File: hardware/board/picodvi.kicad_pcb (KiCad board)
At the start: 4 copper layers, 50 x 30 mm, 55 parts, among them J1 USB_OTG, J2 Conn_01x05, J3 02x06, J4 02x06, J5 NOT_HDMI_A, J6 Conn_01x02, SW1 SW_Push, SW2 SW_Push, SW3 SW_Push, U1 RP2040, U2 NCP115ASN330, U3 W25Q16JV, Y1 12 M

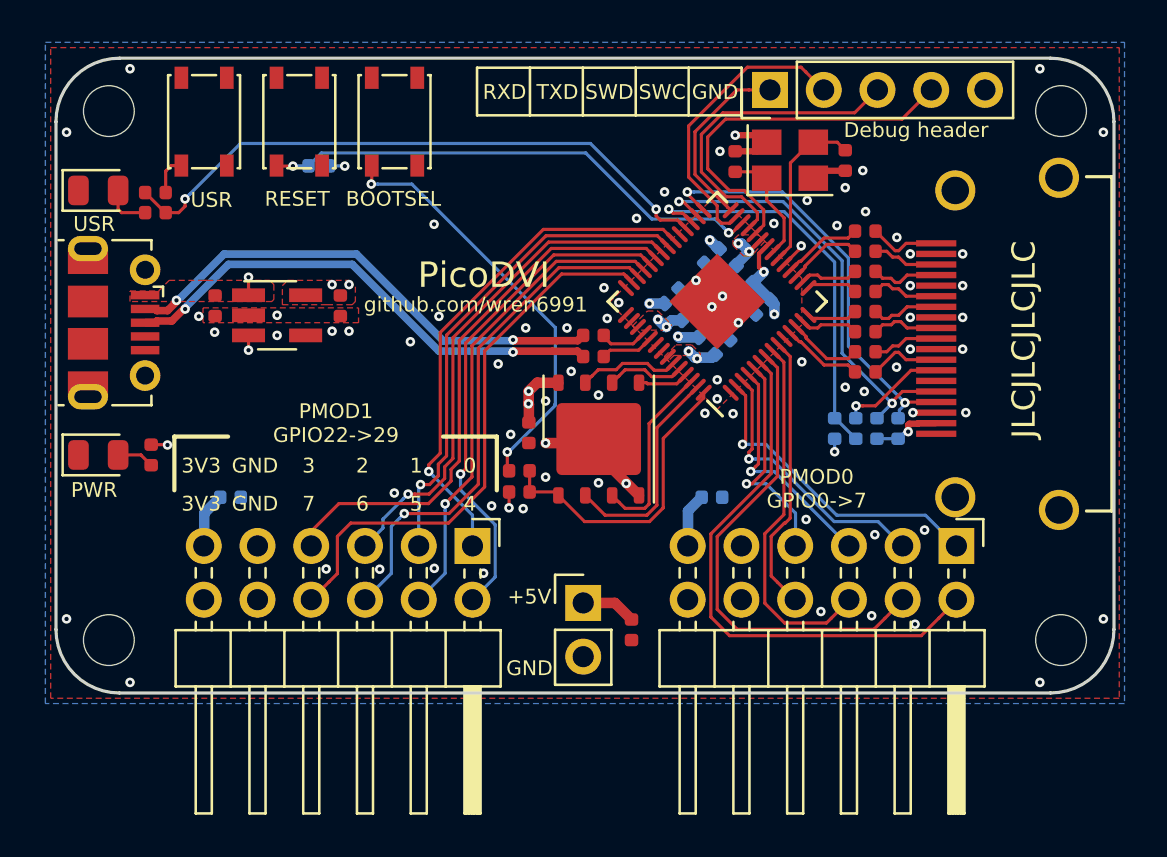
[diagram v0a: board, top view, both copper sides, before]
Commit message: Small updates to PCB
- USB-C
- Silkscreen lables
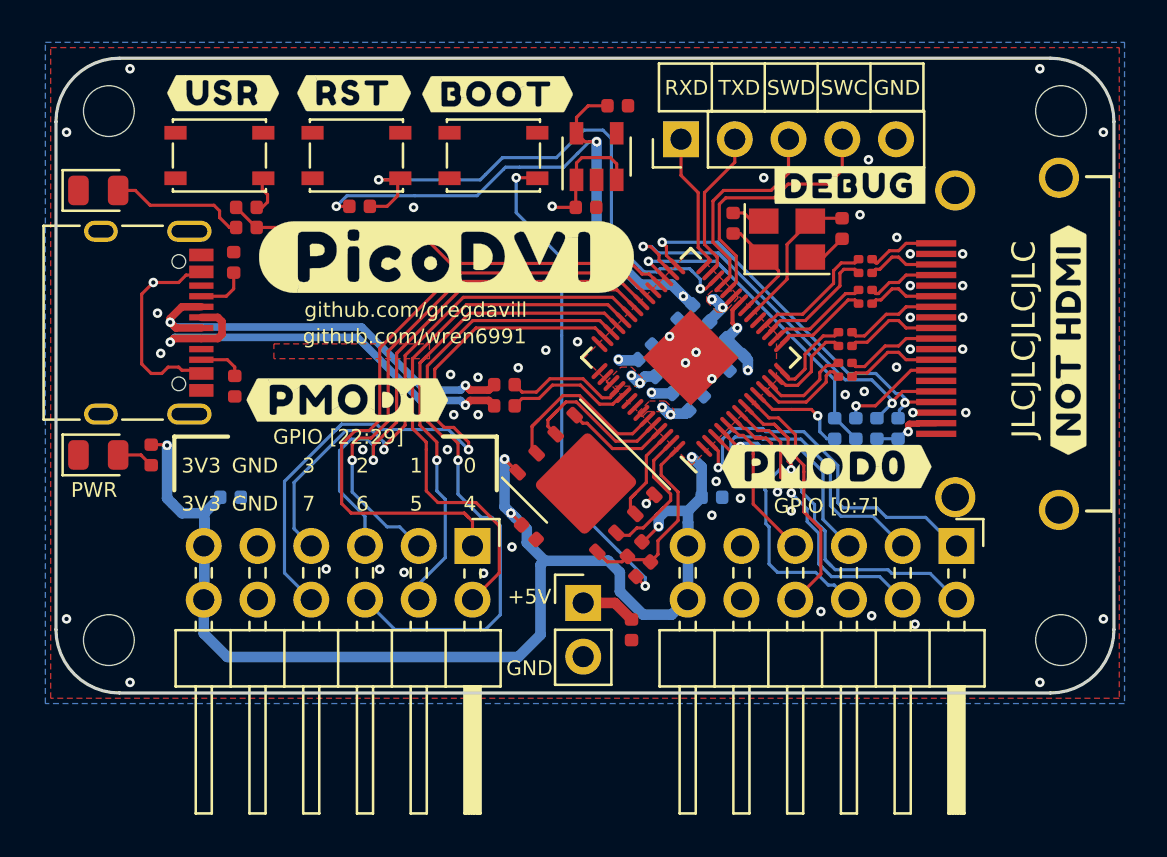
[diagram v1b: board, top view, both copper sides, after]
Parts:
- added ?: , buzzardLabel, F.Cu at (231.4, 104.3)
- added ?: , buzzardLabel, B.Cu at (238.8, 86.5)
- added ?: , buzzardLabel, B.Cu at (225.8, 88.9)
- added ?: , buzzardLabel, B.Cu at (247.8, 103.4)
- added ?: , buzzardLabel, B.Cu at (241.1, 113.3)
- added ?: , buzzardLabel, F.Cu at (217.3, 86.7)
- added ?: , buzzardLabel, F.Cu at (209.0, 101.2)
- added ?: , buzzardLabel, F.Cu at (205.2, 86.7)
- added ?: , buzzardLabel, F.Cu at (247.8, 103.8)
- added ?: , buzzardLabel, F.Cu at (211.4, 86.7)
- added ?: , buzzardLabel, F.Cu at (233.5, 91.0)
- added ?: , buzzardLabel, F.Cu at (209.6, 94.4)
- added ?: , buzzardLabel, B.Cu at (218.1, 113.3)
- added R21: 5k1, Resistor_SMD:R_0402_1005Metric, F.Cu at (208.4, 100.5)
- added R22: 5k1, Resistor_SMD:R_0402_1005Metric, F.Cu at (208.4, 94.7)
- J1: value USB_OTG -> USB_C_Receptacle_USB2.0; footprint Connector_USB:USB_Micro-B_Molex-105017-0001 -> Connector_USB:USB_C_Receptacle_XKB_U262-16XN-4BVC11
- R1: moved to F.Cu
- R12, R13, R14, R15, R16, R17, R18, R19: footprint Resistor_SMD:R_0402_1005Metric -> Resistor_SMD:R_0201_0603Metric
- U2: footprint Package_TO_SOT_SMD:SOT-23-5_HandSoldering -> Package_TO_SOT_SMD:SOT-23-5
- moved C7 18.1 mm to (225.1, 92.0), turned to 0 degrees
- moved U2 16.9 mm to (225.6, 89.7), turned to 90 degrees
- moved C11 16.2 mm to (226.6, 87.2), turned to 0 degrees
- moved R3 7.47 mm to (227.8, 109.2), turned to -135 degrees
- moved R2 6.08 mm to (227.3, 108.2), turned to -135 degrees
- moved SW2 4.94 mm to (220.7, 89.6), turned to 0 degrees
- moved R4 4.81 mm to (221.2, 100.4)
- moved R5 4.81 mm to (221.2, 101.4)
- moved J2 4.81 mm to (229.5, 88.8)
- moved C13 4.70 mm to (222.3, 107.4), turned to -45 degrees
- moved R20 4.36 mm to (209.0, 92.0)
- moved R6 4.36 mm to (209.0, 93.0)
- moved Y1 3.73 mm to (234.6, 93.5)
- moved C12 3.22 mm to (237.2, 93.0)
- moved SW1 3.14 mm to (214.2, 89.6), turned to 0 degrees
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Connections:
- net Net-(J5-Pad14) renamed no_connect_67
- net Net-(J5-Pad19) renamed no_connect_68
- U3 pad 9: GND -> (no net)
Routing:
- net +3V3: track 17.6 -> 100.4 mm, vias 16 -> 13
- net VBUS: track 86.5 -> 126.5 mm
- net /PMOD0_5: track 23.1 -> 14.2 mm, vias 0 -> 1
- net GND: track 12.2 -> 4.04 mm, vias 75 -> 54
- net /PMOD0_4: track 26.1 -> 17.9 mm, vias 0 -> 1
- net /USER_LED_BUTTON: track 29.3 -> 21.5 mm, vias 2 -> 0
- net /UART_TX: track 14.1 -> 7.27 mm
- net /PMOD1_0: track 24.5 -> 31.0 mm, vias 1 -> 0
- net /PMOD1_6: track 24.6 -> 30.8 mm
- net /SWCLK: track 17.8 -> 12.5 mm
- net /SWDIO: track 15.3 -> 10.1 mm
- net /FLASH_~CS~: track 14.4 -> 9.45 mm
- net Net-(D1-Pad2): track 2.23 -> 6.49 mm
- net /PMOD1_7: track 26.5 -> 30.7 mm, vias 0 -> 1
- net /FLASH_SCK: track 3.74 -> 7.88 mm
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- added copper zone on In2.Cu, net GND
- removed copper zone on In2.Cu, net +3V3
- removed copper zone on F.Cu, net VBUS
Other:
- net class Default removed
- net class Tight removed
- net class USB removed
- board text added: "GPIO [0:7]"
- board text added: "GPIO [22:29]"
- board text added: "Rev D"
- board text added: "github.com/gregdavill"
- board text removed: "BOOTSEL"
- board text removed: "Debug header"
- board text removed: "PMOD0"
- board text removed: "PMOD0 GPIO0->7"
- board text removed: "PMOD1"
- board text removed: "PMOD1 GPIO22->29"
- board text removed: "PicoDVI"
- board text removed: "RESET"
- board text removed: "Rev C"
- board text removed: "USR"
